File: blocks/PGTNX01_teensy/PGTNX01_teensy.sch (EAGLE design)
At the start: 43 parts, among them IC1 7805L

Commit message: Committed a load of changes
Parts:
- removed +5V, ON/OFF: HEADER/MALE/01, connectors:HEADER/MALE/01
- added 0, 1, 16, 17, 18, 19, 2, 20, 21, 22, 23, 3, 3.3V, 4, 5, 5V, 6, 7, 8, AVDDIO, AVSSIO, CNV, INT, PIXI_3.3V, PIXI_5V, PIXI_CNV, PIXI_CS, PIXI_GND, PIXI_GND2, PIXI_INT, PIXI_NC1, PIXI_NC2, PIXI_NC3, PIXI_NC4, PIXI_NC5, PIXI_NC6, PIXI_SCK, PIXI_SDI, PIXI_SDO, TNSY_CS, TNSY_MISO, TNSY_MOSI, TNSY_SCK: HEADER/MALE/01, connectors:HEADER/MALE/01
- renumbered CS to 9
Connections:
- new net N$10: CNV.3, PIXI_INT.3, TNSY_15.3
- new net N$11: 18.3, TNSY_18.3
- new net N$12: 19.3, TNSY_19.3
- new net N$13: 20.3, TNSY_20.3
- new net N$14: 21.3, TNSY_21.3
- new net N$15: 22.3, TNSY_22.3
- new net N$16: 23.3, TNSY_23.3
- new net N$17: 0.3, TNSY_0.3
- new net N$18: 1.3, TNSY_1.3
- new net N$19: 2.3, TNSY_2.3
- new net N$2: 17.3, TNSY_17.3
- new net N$20: 3.3, TNSY_3.3
- new net N$21: 4.3, TNSY_4.3
- new net N$22: 5.3, TNSY_5.3
- new net N$23: 6.3, TNSY_6.3
- new net N$24: 7.3, TNSY_7.3
- new net N$25: 8.3, TNSY_8.3
- new net N$26: 9.3, TNSY_9.3
- new net N$3: 3.3V.3, PIXI_3.3V.3, TNSY_3.3V.3
- new net N$4: 16.3, TNSY_16.3
- new net N$5: MOSI.3, PIXI_SDI.3, TNSY_MOSI.3
- new net N$6: MISO.3, PIXI_SDO.3, TNSY_MISO.3
- new net N$7: PIXI_SCK.3, SCK.3, TNSY_SCK.3
- new net N$8: PIXI_CS.3, TNSY_CS.3
- new net N$9: INT.3, PIXI_CNV.3, TNSY_14.3
- net +12V: now also AVDDIO.3
- net -12V: now also AVSSIO.3
- net GND: now also PIXI_GND.3, PIXI_GND2.3, TNSY_GND.3
- net N$1: now also 5V.3, PIXI_5V.3, TNSY_VIN.3; no longer +5V.3
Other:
- moved on the sheet: C3, IC1, MISO, MOSI, SCK, TNSY_0, TNSY_1, TNSY_14, TNSY_15, TNSY_16, TNSY_17, TNSY_18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

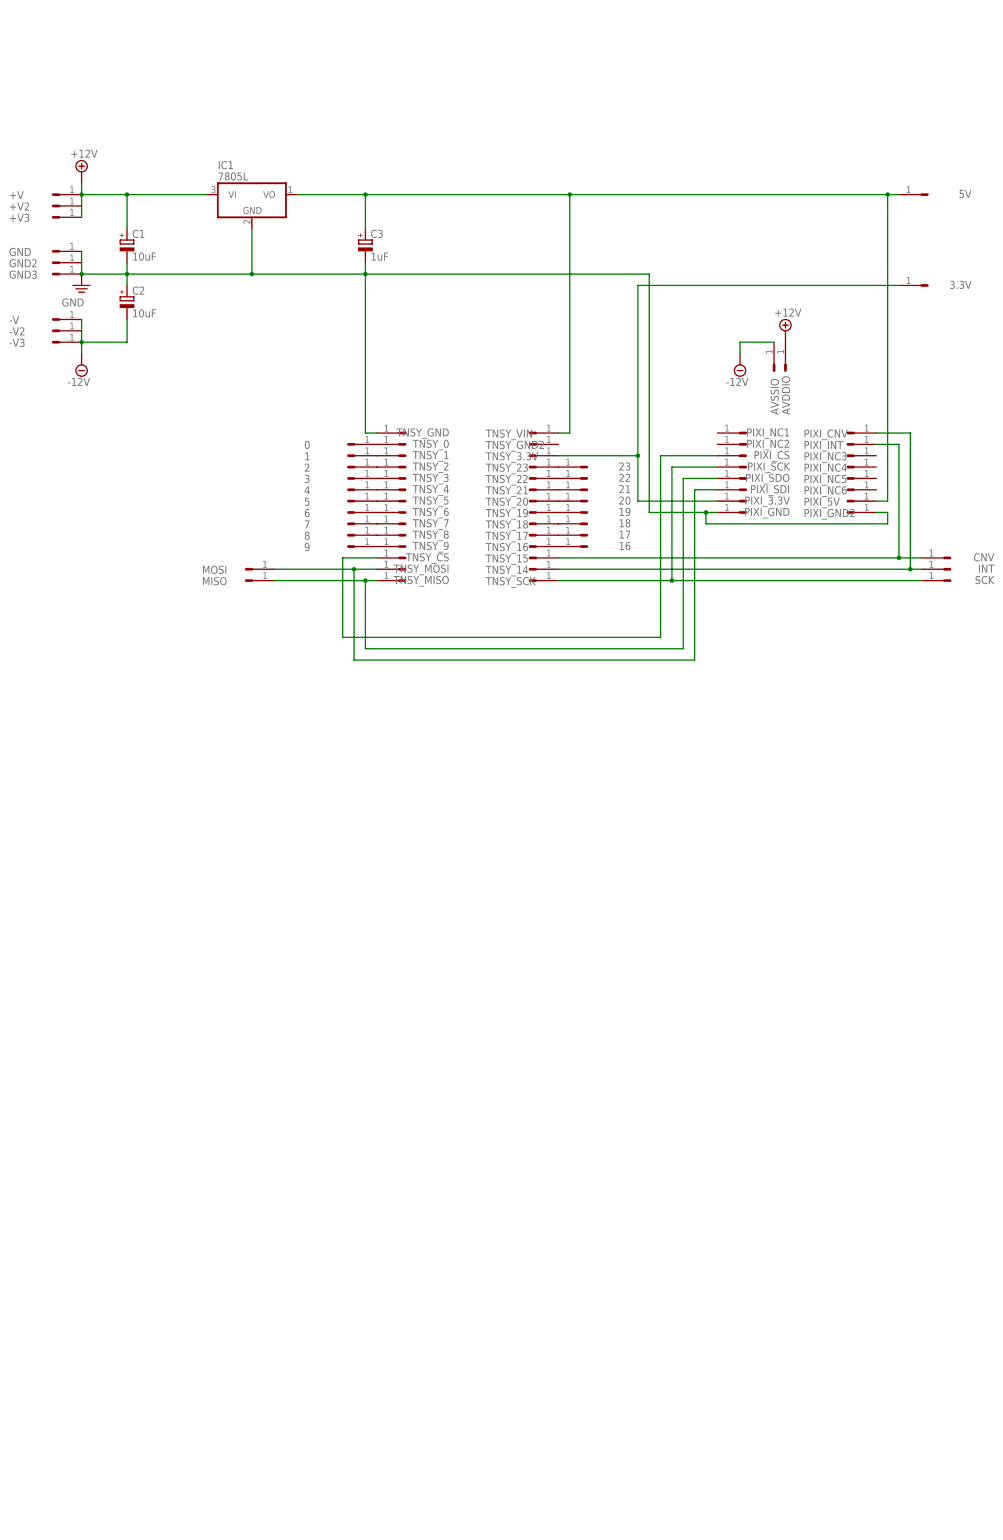
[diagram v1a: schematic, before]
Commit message: Added output resistors and xener voltage limiters.
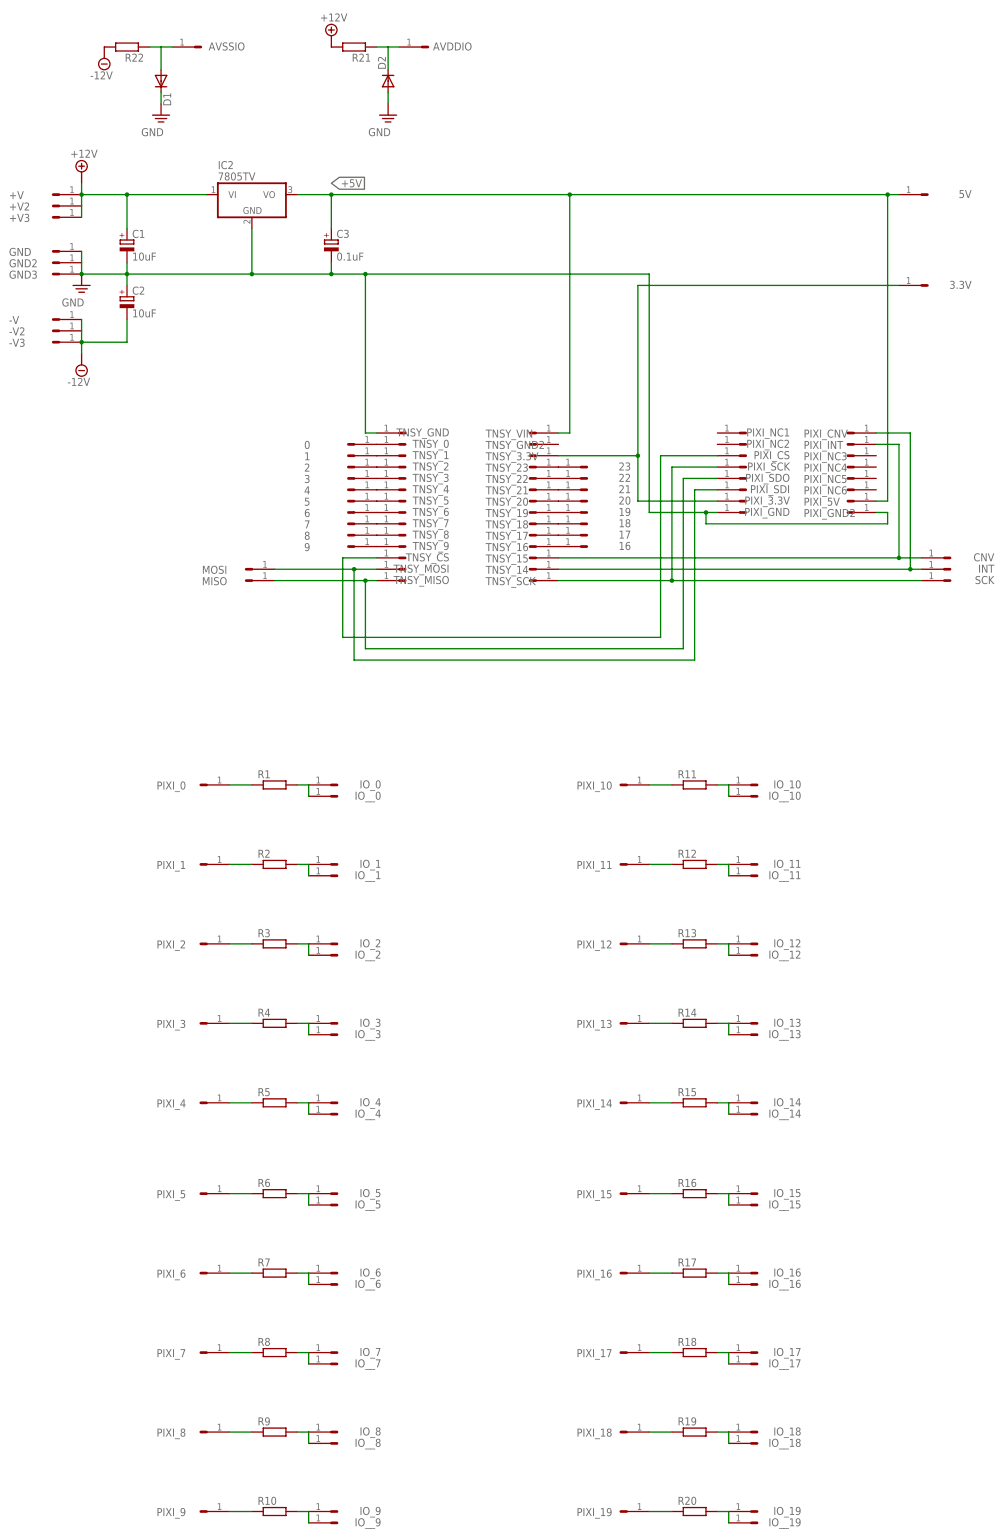
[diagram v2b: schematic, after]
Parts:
- removed IC1: 7805L, ic_voltage_reg:7805L
- added D1, D2: (no value), transistors:1N4148DO35-7
- added IC2: 7805TV, ic_voltage_reg:7805TV
- added IO_0, IO_1, IO_10, IO_11, IO_12, IO_13, IO_14, IO_15, IO_16, IO_17, IO_18, IO_19, IO_2, IO_3, IO_4, IO_5, IO_6, IO_7, IO_8, IO_9, IO__0, IO__1, IO__10, IO__11, IO__12, IO__13, IO__14, IO__15, IO__16, IO__17, IO__18, IO__19, IO__2, IO__3, IO__4, IO__5, IO__6, IO__7, IO__8, IO__9, PIXI_0, PIXI_1, PIXI_10, PIXI_11, PIXI_12, PIXI_13, PIXI_14, PIXI_15, PIXI_16, PIXI_17, PIXI_18, PIXI_19, PIXI_2, PIXI_3, PIXI_4, PIXI_5, PIXI_6, PIXI_7, PIXI_8, PIXI_9: HEADER/MALE/01, connectors:HEADER/MALE/01
- added R1, R10, R11, R12, R13, R14, R15, R16, R17, R18, R19, R2, R20, R21, R22, R3, R4, R5, R6, R7, R8, R9: (no value), resistors:RESISTORRESISTOR/UPRIGHT/7.5
- C3: value 1uF -> 0.1uF
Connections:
- new net +5V: 5V.3, C3.+, IC2.VO, PIXI_5V.3, TNSY_VIN.3
- new net N$27: IO_1.3, IO__1.3, R2.2
- new net N$29: IO_0.3, IO__0.3, R1.2
- new net N$3: PIXI_1.3, R2.1
- new net N$30: PIXI_2.3, R3.1
- new net N$31: IO_2.3, IO__2.3, R3.2
- new net N$32: PIXI_3.3, R4.1
- new net N$33: IO_3.3, IO__3.3, R4.2
- new net N$34: PIXI_4.3, R5.1
- new net N$35: IO_4.3, IO__4.3, R5.2
- new net N$36: PIXI_5.3, R6.1
- new net N$37: IO_5.3, IO__5.3, R6.2
- new net N$38: PIXI_6.3, R7.1
- new net N$39: IO_6.3, IO__6.3, R7.2
- new net N$40: PIXI_7.3, R8.1
- new net N$41: IO_7.3, IO__7.3, R8.2
- new net N$42: PIXI_8.3, R9.1
- new net N$43: IO_8.3, IO__8.3, R9.2
- new net N$44: PIXI_9.3, R10.1
- new net N$45: IO_9.3, IO__9.3, R10.2
- new net N$46: PIXI_10.3, R11.1
- new net N$47: IO_10.3, IO__10.3, R11.2
- new net N$48: PIXI_11.3, R12.1
- new net N$49: IO_11.3, IO__11.3, R12.2
- new net N$50: PIXI_12.3, R13.1
- new net N$51: IO_12.3, IO__12.3, R13.2
- new net N$52: PIXI_13.3, R14.1
- new net N$53: IO_13.3, IO__13.3, R14.2
- new net N$54: PIXI_14.3, R15.1
- new net N$55: IO_14.3, IO__14.3, R15.2
- new net N$56: PIXI_15.3, R16.1
- new net N$57: IO_15.3, IO__15.3, R16.2
- new net N$58: PIXI_16.3, R17.1
- new net N$59: IO_16.3, IO__16.3, R17.2
- new net N$60: PIXI_17.3, R18.1
- new net N$61: IO_17.3, IO__17.3, R18.2
- new net N$62: PIXI_18.3, R19.1
- new net N$63: IO_18.3, IO__18.3, R19.2
- new net N$64: PIXI_19.3, R20.1
- new net N$65: IO_19.3, IO__19.3, R20.2
- new net N$66: AVDDIO.3, D2.C, R21.1
- new net N$67: AVSSIO.3, D1.A, R22.1
- net +12V: now also IC2.VI, R21.2; no longer AVDDIO.3, IC1.VI
- net -12V: now also R22.2; no longer AVSSIO.3
- net GND: now also D1.C, D2.A, IC2.GND; no longer IC1.GND
- net N$1: now also PIXI_0.3, R1.1; no longer 5V.3, C3.+, IC1.VO, PIXI_5V.3, TNSY_VIN.3
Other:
- moved on the sheet: AVDDIO, AVSSIO, C3

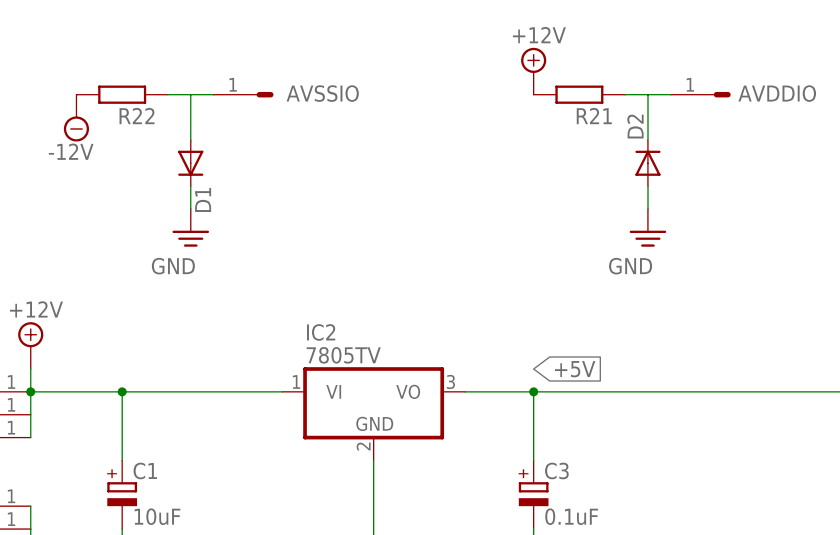
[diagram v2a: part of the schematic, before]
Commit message: Added correct diode type BZX55C12
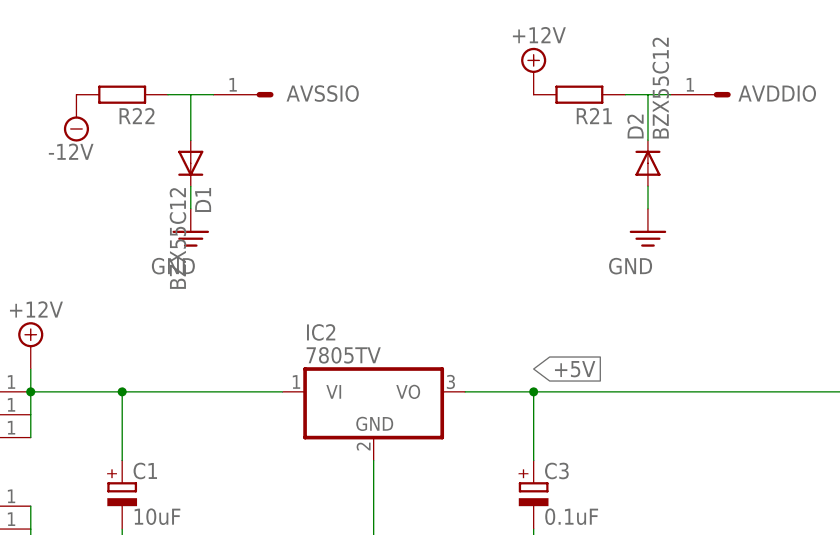
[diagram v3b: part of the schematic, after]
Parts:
- D1, D2: value (none) -> BZX55C12
